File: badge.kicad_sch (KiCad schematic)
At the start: 23 parts, among them SW1 SW_Push, SW2 SW_Push, SW3 SW_Push, SW4 SW_Push, SW5 SW_Push, U1 NHD-C12832A1Z-FSRGB-FBW-3V

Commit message: now we start layout
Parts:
- BT1: footprint (none) -> Battery:BatteryHolder_Keystone_2479_3xAAA
- C1, C2, C3, C4, C5: footprint (none) -> Capacitor_THT:C_Disc_D5.0mm_W2.5mm_P5.00mm
- C6, C7, C8: footprint (none) -> Capacitor_THT:CP_Radial_D5.0mm_P2.50mm
- D1: footprint (none) -> Diode_THT:D_DO-35_SOD27_P10.16mm_Horizontal
- D2, D3, D4: footprint (none) -> LED_THT:LED_D3.0mm
- R3, R4, R5: footprint (none) -> Resistor_THT:R_Axial_DIN0207_L6.3mm_D2.5mm_P10.16mm_Horizontal
- SW1, SW2, SW3, SW4, SW5: footprint (none) -> Button_Switch_THT:SW_PUSH_6mm
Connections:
- net GND: now also C1.1, C2.1, C3.1, C4.1, C5.1
- net at C5.2: now also U1.5 (V4)
- net at C4.2: now also U1.4 (V3)
- net at U1.1 (V0): now also C1.2
- net at U1.2 (V1): now also C2.2
- net at U1.3 (V2): now also C3.2
- no-connect marks 2 -> 0
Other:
- moved on the sheet: C1, C2, C3, C4, C5, SW1, SW2, SW3, SW4, SW5

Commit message: work has been proceding
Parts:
- U1: footprint NHD-C12_NDI -> FTbadge:NHD-C12_NDI
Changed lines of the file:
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@@
 			)
 		)
-		(property "Footprint" "NHD-C12_NDI"
+		(property "Footprint" "FTbadge:NHD-C12_NDI"
 			(at 184.15 46.99 0)
 			(hide yes)

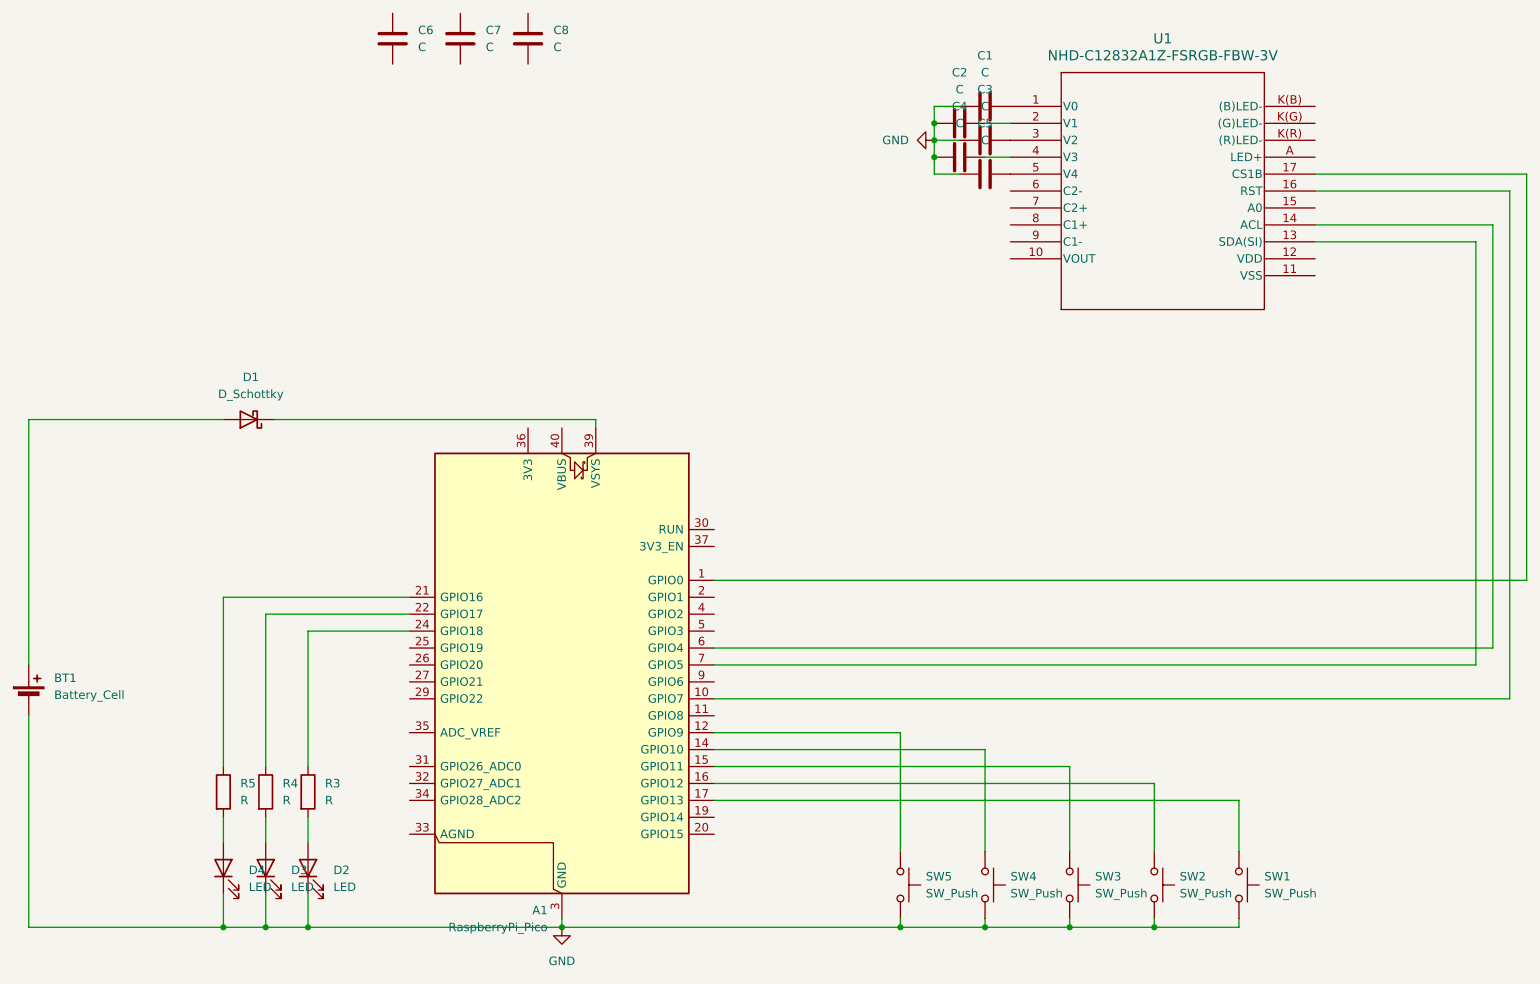
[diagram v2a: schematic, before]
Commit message: schematic: add +3V3, electrolytics, RGB cathodes
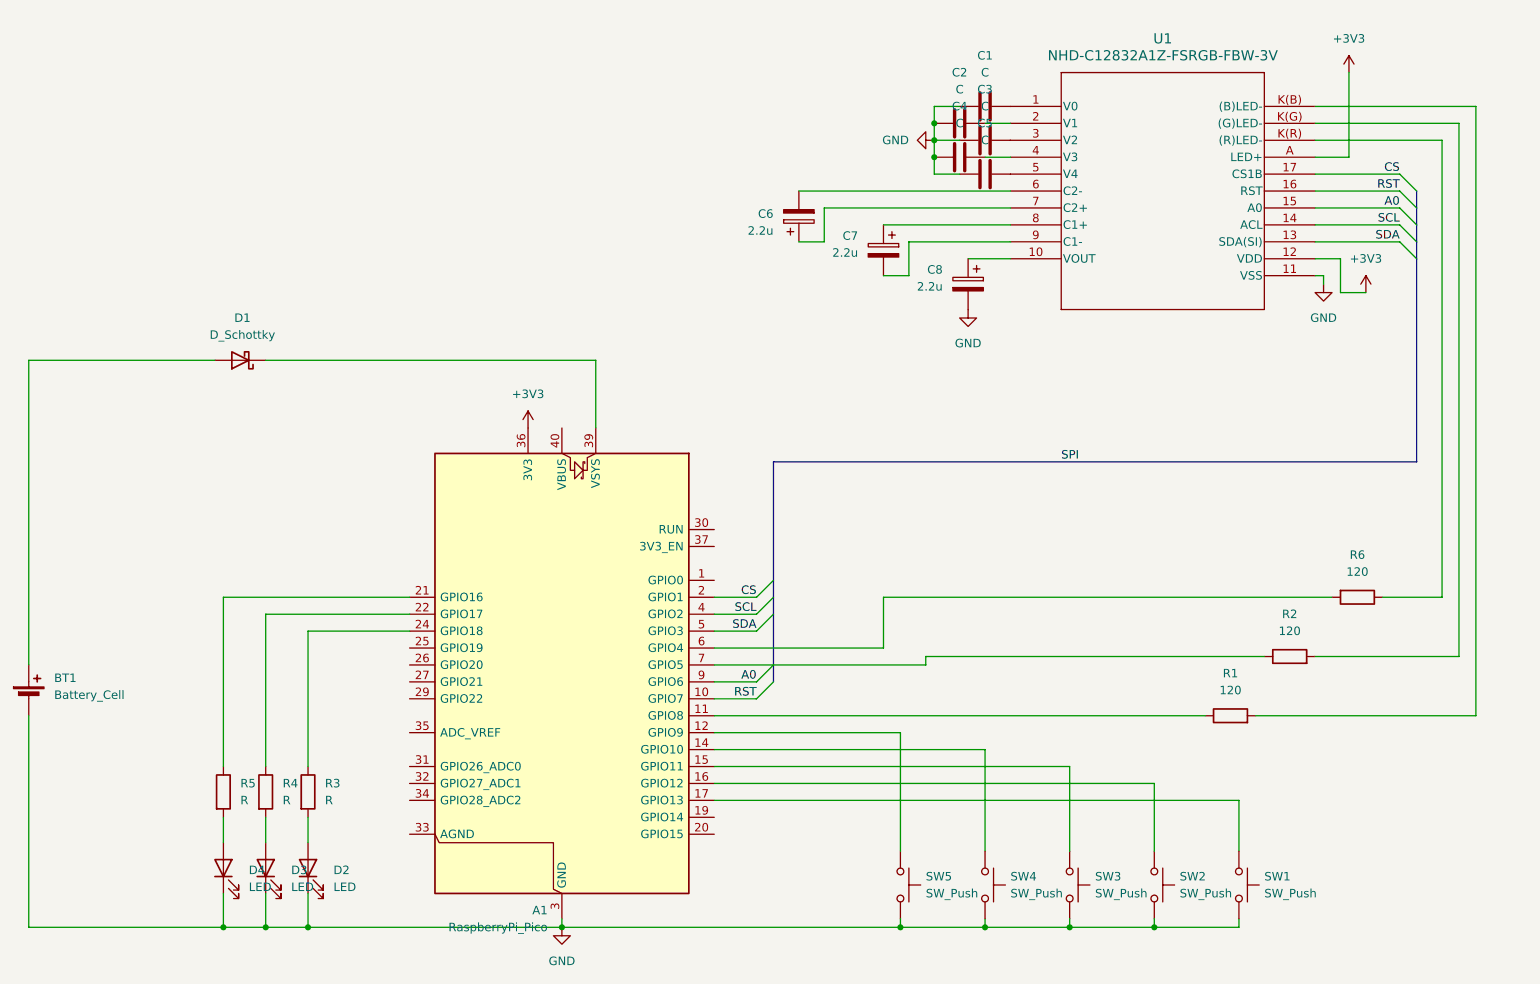
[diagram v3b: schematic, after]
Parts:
- removed C6, C7, C8: C, Capacitor_THT:CP_Radial_D5.0mm_P2.50mm, symbol Device:C
- added C6, C7, C8: 2.2u, symbol Device:C_Polarized
- added R1, R2, R6: 120, symbol Device:R
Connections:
- net GND: now also U1.11 (VSS), C8.2
- net at A1.1 (GPIO0): no longer U1.17 (CS1B)
- net RST: now reaches A1.10 (GPIO7), U1.16 (RST)
- net at A1.11 (GPIO8): now also R1.1
- net CS: now reaches A1.2 (GPIO1)
- net CS: now also U1.17 (CS1B)
- net +3V3: now reaches A1.36 (3V3)
- net +3V3: now also U1.12 (VDD), U1.A (LED+)
- net SCL: now reaches A1.4 (GPIO2)
- net SCL: now also U1.14 (ACL)
- net SDA: now reaches A1.5 (GPIO3)
- net SDA: now also U1.13 (SDA(SI))
- net at A1.6 (GPIO4): now also R6.2; no longer U1.14 (ACL)
- net at A1.7 (GPIO5): now also R2.1; no longer U1.13 (SDA(SI))
- net A0: now reaches A1.9 (GPIO6)
- net A0: now also U1.15 (A0)
- net at U1.10 (VOUT): now also C8.1
- net at U1.6 (C2-): now also C6.2
- net at U1.7 (C2+): now also C6.1
- net at U1.8 (C1+): now also C7.1
- net at U1.9 (C1-): now also C7.2
- net at U1.K(B) ((B)LED-): now also R1.2
- net at U1.K(G) ((G)LED-): now also R2.2
- net at U1.K(R) ((R)LED-): now also R6.1
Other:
- moved on the sheet: D1

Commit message: Remove Hole
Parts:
- C6, C7, C8: footprint (none) -> Capacitor_THT:CP_Radial_D5.0mm_P2.00mm
- R1, R2, R6: footprint (none) -> Resistor_THT:R_Axial_DIN0207_L6.3mm_D2.5mm_P10.16mm_Horizontal
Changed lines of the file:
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@@
 			)
 		)
-		(property "Footprint" ""
+		(property "Footprint" "Resistor_THT:R_Axial_DIN0207_L6.3mm_D2.5mm_P10.16mm_Horizontal"
 			(at 236.22 118.872 90)
 			(hide yes)
@@
 			)
 		)
-		(property "Footprint" ""
+		(property "Footprint" "Capacitor_THT:CP_Radial_D5.0mm_P2.00mm"
 			(at 164.1348 72.39 0)
 			(hide yes)
@@
 			)
 		)
-		(property "Footprint" ""
+		(property "Footprint" "Resistor_THT:R_Axial_DIN0207_L6.3mm_D2.5mm_P10.16mm_Horizontal"
 			(at 217.17 140.208 90)
 			(hide yes)
@@
 			)
 		)
-		(property "Footprint" ""
+		(property "Footprint" "Capacitor_THT:CP_Radial_D5.0mm_P2.00mm"
 			(at 153.3652 59.69 0)
 			(hide yes)
@@
 			)
 		)
-		(property "Footprint" ""
+		(property "Footprint" "Capacitor_THT:CP_Radial_D5.0mm_P2.00mm"
 			(at 176.8348 77.47 0)
 			(hide yes)
@@
 			)
 		)
-		(property "Footprint" ""
+		(property "Footprint" "Resistor_THT:R_Axial_DIN0207_L6.3mm_D2.5mm_P10.16mm_Horizontal"
 			(at 226.06 131.318 90)
 			(hide yes)

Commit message: Dots: Connected
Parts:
- A1: footprint Module:RaspberryPi_Pico_Common_Unspecified -> Module:RaspberryPi_Pico_Common_SMD
- BT1: footprint Battery:BatteryHolder_Keystone_2479_3xAAA -> FTbadge:BatteryHolder_Keystone_2479_3xAAA_NoHole
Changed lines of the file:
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@@
 			)
 		)
-		(property "Footprint" "Battery:BatteryHolder_Keystone_2479_3xAAA"
+		(property "Footprint" "FTbadge:BatteryHolder_Keystone_2479_3xAAA_NoHole"
 			(at 36.83 134.366 90)
 			(hide yes)
@@
 			)
 		)
-		(property "Footprint" "Module:RaspberryPi_Pico_Common_Unspecified"
+		(property "Footprint" "Module:RaspberryPi_Pico_Common_SMD"
 			(at 116.84 180.34 0)
 			(hide yes)

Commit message: pawsgit push
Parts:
- added J1: TC2030, FTbadge:Paw-Connect_RevB_TC2030-IDC-NL_2x03_P1.27mm_Vertical, symbol Connector:TC2030
- A1: footprint Module:RaspberryPi_Pico_Common_SMD -> Module:RaspberryPi_Pico_SMD_HandSolder; symbol MCU_Module:RaspberryPi_Pico -> MCU_Module:RaspberryPi_Pico_Debug
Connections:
- net GND: now also A1.D2 (GND), J1.5
- net at A1.30 (RUN): now also J1.3
- new net: A1.D3 (SWDIO), J1.2
- new net: A1.D1 (SWCLK), J1.4
- no-connect marks 0 -> 2

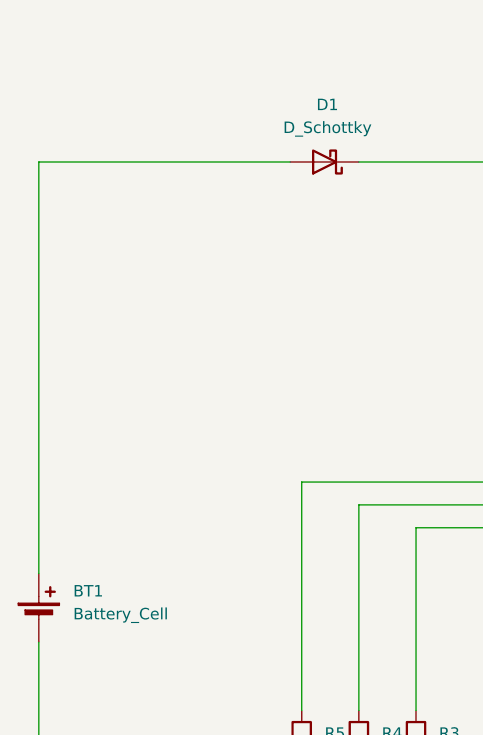
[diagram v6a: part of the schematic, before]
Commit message: board can be turned off
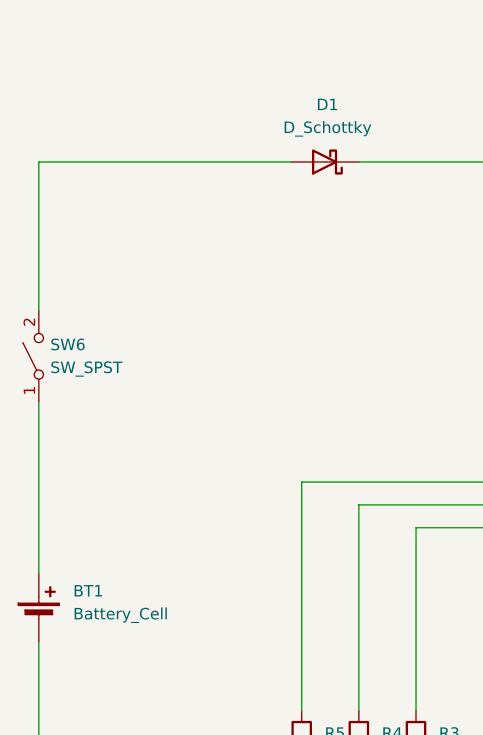
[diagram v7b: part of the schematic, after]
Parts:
- added SW6: SW_SPST, FTbadge:SW_SLW-1277744-3A-N-D, symbol Switch:SW_SPST
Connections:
- net at D1.2 (A): now also SW6.2 (B); no longer BT1.1 (+)
- new net: BT1.1 (+), SW6.1 (A)
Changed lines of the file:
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@@
 	(wire
 		(pts
+			(xy 36.83 101.6) (xy 36.83 85.09)
+		)
+		(stroke
+			(width 0)
+			(type default)
+		)
+	)
+	(wire
+		(pts
 			(xy 139.7 57.15) (xy 139.7 102.87)
 		)
@@
 	(wire
 		(pts
-			(xy 36.83 130.81) (xy 36.83 85.09)
+			(xy 36.83 130.81) (xy 36.83 111.76)
 		)
 		(stroke
@@
 					(unit 1)
 				)
+			)
+		)
+	)
+	(symbol
+		(lib_id "Switch:SW_SPST")
+		(at 36.83 106.68 90)
+		(unit 1)
+		(body_style 1)
+		(exclude_from_sim no)
+		(in_bom yes)
+		(on_board yes)
+		(in_pos_files yes)
+		(dnp no)
+		(fields_autoplaced yes)
+		(property "Reference" "SW6"
+			(at 38.1 105.4099 90)
+			(show_name no)
+			(do_not_autoplace no)
+			(effects
+				(font
+					(size 1.27 1.27)
+				)
+				(justify right)
+			)
+		)
+		(property "Value" "SW_SPST"
+			(at 38.1 107.9499 90)
+			(show_name no)
+			(do_not_autoplace no)
+			(effects
+				(font
+					(size 1.27 1.27)
+				)
+				(justify right)
+			)
+		)
+		(property "Footprint" "FTbadge:SW_SLW-1277744-3A-N-D"
+			(at 36.83 106.68 0)
+			(hide yes)
+			(show_name no)
+			(do_not_autoplace no)
+			(effects
+				(font
+					(size 1.27 1.27)
+				)
+			)
+		)
+		(property "Datasheet" ""
+			(at 36.83 106.68 0)
+			(hide yes)
+			(show_name no)
+			(do_not_autoplace no)
+			(effects
+				(font
+					(size 1.27 1.27)
+				)
+			)
+		)
+		(property "Description" "Single Pole Single Throw (SPST) switch"
+			(at 36.83 106.68 0)
+			(hide yes)
+			(show_name no)
+			(do_not_autoplace no)
+			(effects
+				(font
+					(size 1.27 1.27)
+				)
+			)
+		)
+		(pin "1"
+		)
+		(pin "2"
+		)
+		(instances
+			(project "badge"
+				(path "/1e376a43-e2df-41cb-8688-d8f95da10731"
+					(reference "SW6")
+					(unit 1)
+				)

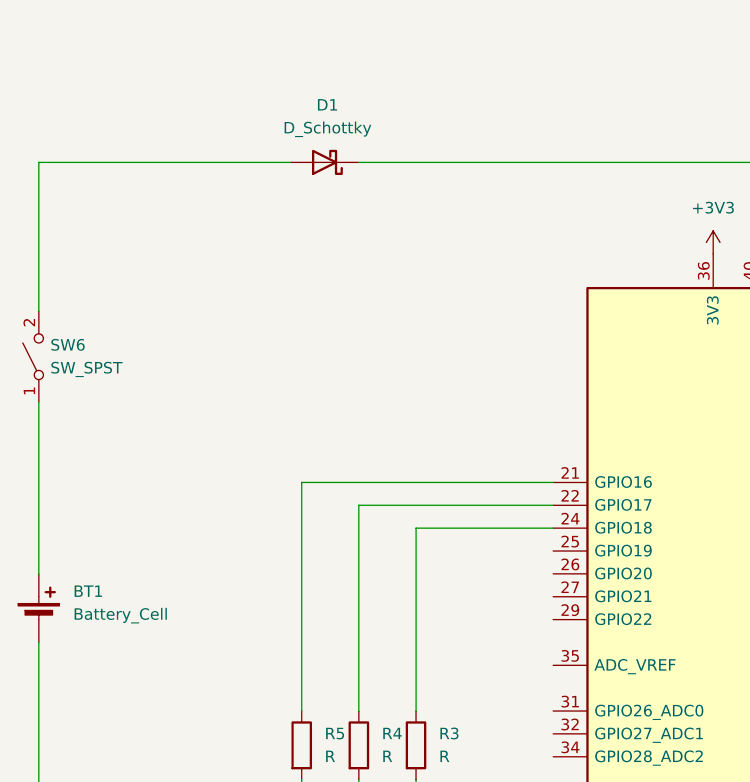
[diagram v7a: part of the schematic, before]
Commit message: Add SAO connector
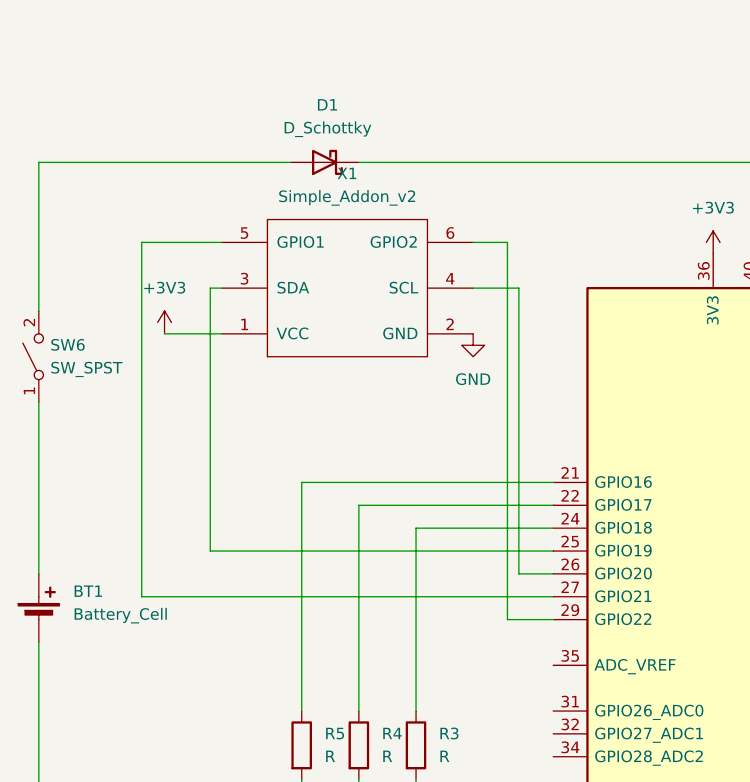
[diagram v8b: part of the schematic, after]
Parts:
- added X1: Simple_Addon_v2, FTbadge:Simple_Addon_v2-BADGE-2x3, symbol FurryTel:Simple_Addon_v2
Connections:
- net +3V3: now also X1.1 (VCC)
- net GND: now also X1.2 (GND)
- net at A1.25 (GPIO19): now also X1.3 (SDA)
- net at A1.26 (GPIO20): now also X1.4 (SCL)
- net at A1.27 (GPIO21): now also X1.5 (GPIO1)
- net at A1.29 (GPIO22): now also X1.6 (GPIO2)
